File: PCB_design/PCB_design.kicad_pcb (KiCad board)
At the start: 2 copper layers, 39 parts, among them J1 USB_B_Micro, J4 Conn_01x02_Pin, Q1 FS8205A, U1 L298N, U2 L7805, U3 TP4056, U4 DW01A

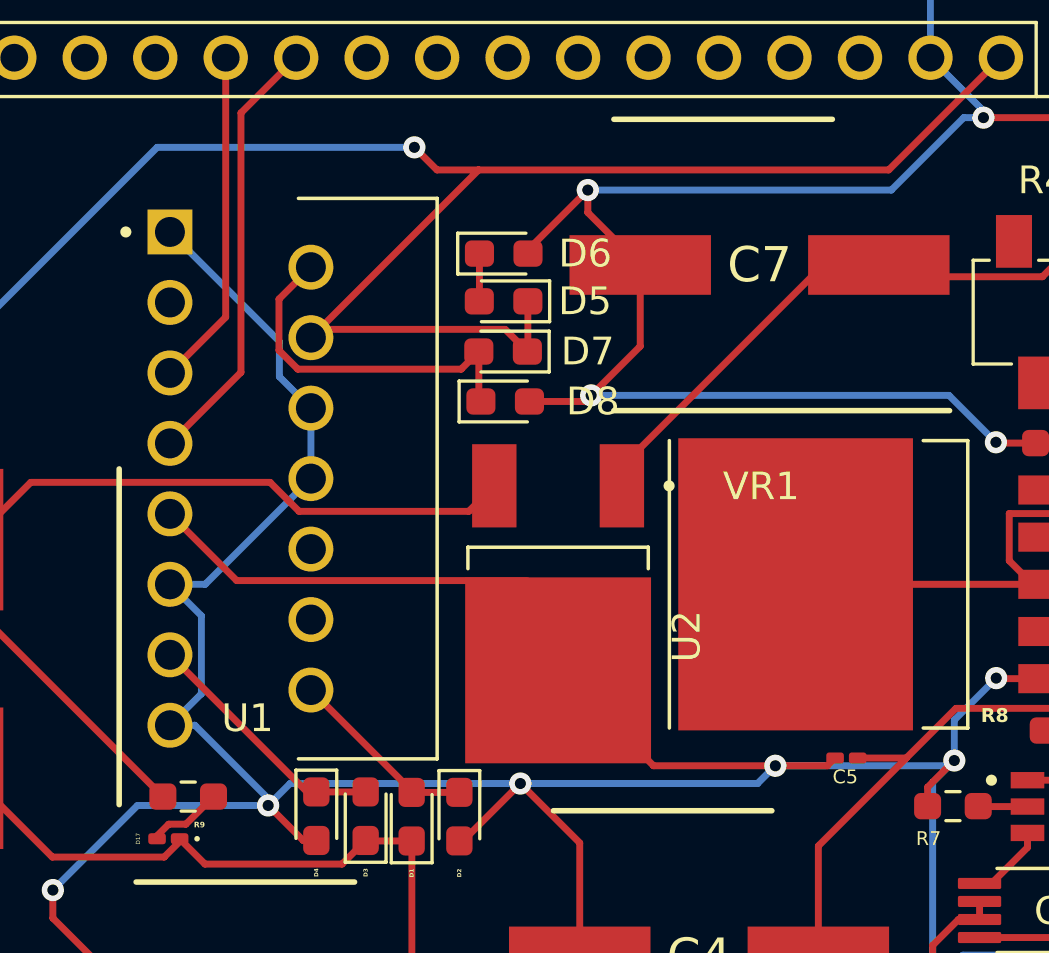
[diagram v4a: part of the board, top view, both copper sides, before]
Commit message: Fixed issues surrounding wiring, Vss to Vs for 12V, CE actually enabled
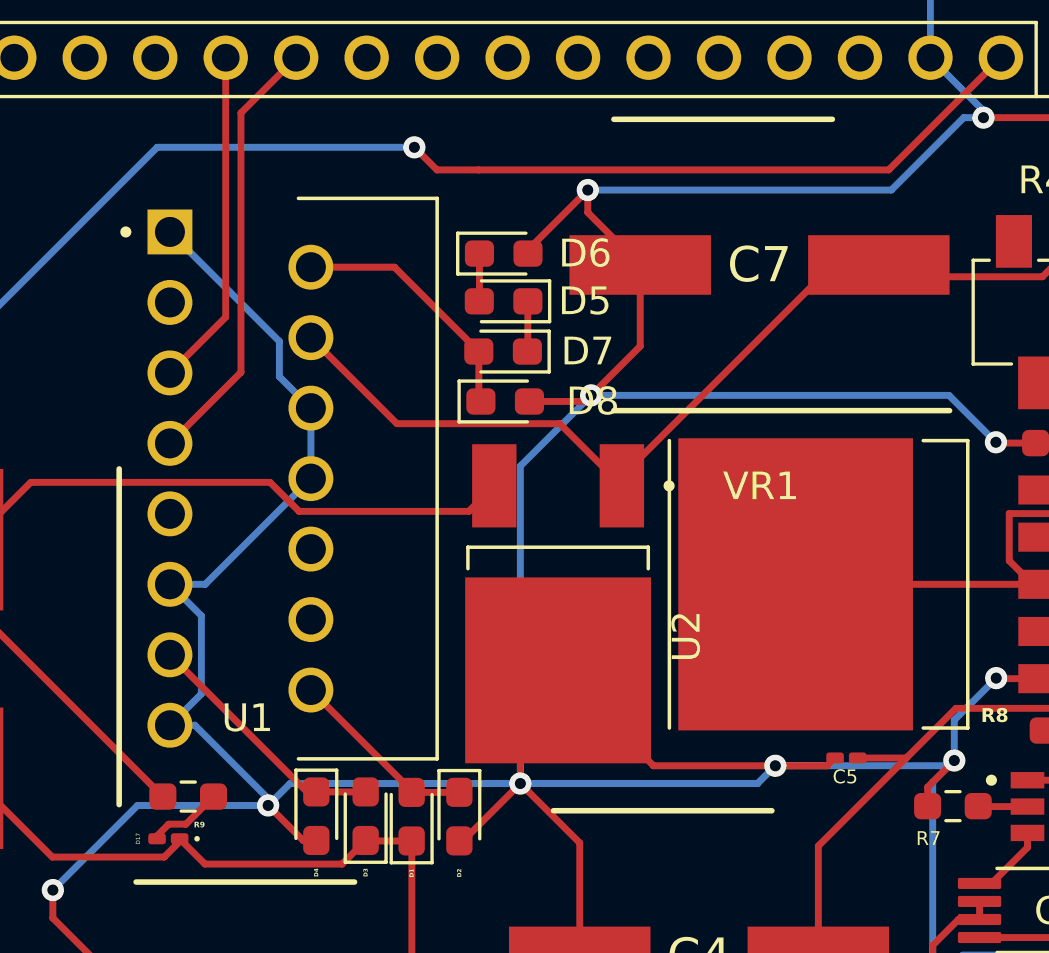
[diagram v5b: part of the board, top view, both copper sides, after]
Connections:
- U1 pad 4: +5V -> Boost_Out
- U1 pad 9: GND_Out -> +5V
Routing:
- net +5V: track 104.3 -> 87.5 mm
- net Boost_Out: track 28.5 -> 44.5 mm
- net GND_Out: track 232.0 -> 237.8 mm
- net OUT1: track 13.0 -> 9.14 mm
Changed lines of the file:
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@@
       (net 37 "OUT2") (pinfunction "OUT2") (pintype "output") (solder_mask_margin 0.102))
     (pad "4" thru_hole circle (at 5.08 3.81) (size 1.62 1.62) (drill 1.08) (layers "*.Cu" "*.Mask")
-      (net 28 "+5V") (pinfunction "Vs") (pintype "power_in") (solder_mask_margin 0.102))
+      (net 31 "Boost_Out") (pinfunction "Vs") (pintype "power_in") (solder_mask_margin 0.102))
     (pad "5" thru_hole circle (at 0 5.08) (size 1.62 1.62) (drill 1.08) (layers "*.Cu" "*.Mask")
       (net 18 "Net-(A1-A0)") (pinfunction "IN1") (pintype "input") (solder_mask_margin 0.102))
@@
       (net 61 "GND_Out") (pinfunction "GND") (pintype "power_in") (solder_mask_margin 0.102))
     (pad "9" thru_hole circle (at 0 10.16) (size 1.62 1.62) (drill 1.08) (layers "*.Cu" "*.Mask")
-      (net 61 "GND_Out") (pinfunction "Vss") (pintype "power_in") (solder_mask_margin 0.102))
+      (net 28 "+5V") (pinfunction "Vss") (pintype "power_in") (solder_mask_margin 0.102))
     (pad "10" thru_hole circle (at 5.08 11.43) (size 1.62 1.62) (drill 1.08) (layers "*.Cu" "*.Mask")
       (net 56 "unconnected-(U1-IN3-Pad10)") (pinfunction "IN3") (pintype "input") (solder_mask_margin 0.102))
@@
   (segment (start 145.36125 91.3) (end 143.7215 91.3) (width 0.25) (layer "F.Cu") (net 28))
   (segment (start 137 91.323541) (end 136.443541 91.88) (width 0.25) (layer "F.Cu") (net 28))
-  (segment (start 149.5325 73.66) (end 148.7325 72.86) (width 0.25) (layer "F.Cu") (net 28))
   (segment (start 145.37 97.64) (end 144.98 98.03) (width 0.25) (layer "F.Cu") (net 28))
   (segment (start 132.41 91.88) (end 129.57 89.04) (width 0.25) (layer "F.Cu") (net 28))
@@
   (segment (start 147.775 67.115) (end 146.275 67.115) (width 0.25) (layer "F.Cu") (net 28))
   (segment (start 137.9125 92.1325) (end 142.854 92.1325) (width 0.25) (layer "F.Cu") (net 28))
-  (segment (start 147.775 67.115) (end 141.73 73.16) (width 0.25) (layer "F.Cu") (net 28))
   (segment (start 146.275 67.115) (end 145.46 66.3) (width 0.25) (layer "F.Cu") (net 28))
   (segment (start 149.55 71.85) (end 149.55 73.6425) (width 0.25) (layer "F.Cu") (net 28))
@@
   (segment (start 145.37 91.30875) (end 145.37 97.64) (width 0.25) (layer "F.Cu") (net 28))
   (segment (start 137 91.22) (end 137 91.323541) (width 0.25) (layer "F.Cu") (net 28))
-  (segment (start 148.7325 72.86) (end 142.03 72.86) (width 0.25) (layer "F.Cu") (net 28))
   (segment (start 149.55 73.6425) (end 149.5325 73.66) (width 0.25) (layer "F.Cu") (net 28))
   (segment (start 137 91.22) (end 137.9125 92.1325) (width 0.25) (layer "F.Cu") (net 28))
   (segment (start 136.443541 91.88) (end 132.41 91.88) (width 0.25) (layer "F.Cu") (net 28))
-  (segment (start 142.03 72.86) (end 141.73 73.16) (width 0.25) (layer "F.Cu") (net 28))
   (segment (start 142.854 92.1325) (end 143.704 91.2825) (width 0.25) (layer "F.Cu") (net 28))
   (segment (start 145.36125 91.3) (end 145.37 91.30875) (width 0.25) (layer "F.Cu") (net 28))
@@
   (segment (start 169.15 86.52) (end 169.95 87.32) (width 0.25) (layer "F.Cu") (net 30))
   (segment (start 162.625 70.965) (end 168.095 70.965) (width 0.25) (layer "F.Cu") (net 31))
+  (segment (start 141.73 73.16) (end 144.83 76.26) (width 0.25) (layer "F.Cu") (net 31))
   (segment (start 174.27 71.08) (end 171.74 71.08) (width 0.25) (layer "F.Cu") (net 31))
   (segment (start 170.76 71.08) (end 169.37 69.69) (width 0.25) (layer "F.Cu") (net 31))
   (segment (start 171.74 68.86) (end 171.74 71.08) (width 0.25) (layer "F.Cu") (net 31))
   (segment (start 168.095 70.965) (end 169.37 69.69) (width 0.25) (layer "F.Cu") (net 31))
+  (segment (start 152.94 78.5) (end 152.94 78.15) (width 0.25) (layer "F.Cu") (net 31))
   (segment (start 160.2 70.54) (end 162.2 70.54) (width 0.25) (layer "F.Cu") (net 31))
-  (segment (start 152.94 77.8) (end 160.2 70.54) (width 0.25) (layer "F.Cu") (net 31))
+  (segment (start 160.55 70.54) (end 162.2 70.54) (width 0.25) (layer "F.Cu") (net 31))
   (segment (start 152.94 78.5) (end 152.94 77.8) (width 0.25) (layer "F.Cu") (net 31))
   (segment (start 171.74 71.08) (end 170.76 71.08) (width 0.25) (layer "F.Cu") (net 31))
+  (segment (start 152.94 78.15) (end 160.55 70.54) (width 0.25) (layer "F.Cu") (net 31))
   (segment (start 162.2 70.54) (end 162.625 70.965) (width 0.25) (layer "F.Cu") (net 31))
+  (segment (start 150.7 76.26) (end 152.94 78.5) (width 0.25) (layer "F.Cu") (net 31))
+  (segment (start 144.83 76.26) (end 150.7 76.26) (width 0.25) (layer "F.Cu") (net 31))
   (segment (start 170.42925 101.66) (end 170.42725 101.662) (width 0.25) (layer "F.Cu") (net 32))
   (segment (start 166.35225 100.709) (end 167.30325 101.66) (width 0.25) (layer "F.Cu") (net 32))
@@
   (segment (start 147.805 70.13) (end 147.805 71.845) (width 0.25) (layer "F.Cu") (net 37))
   (segment (start 147.805 71.845) (end 147.8 71.85) (width 0.25) (layer "F.Cu") (net 37))
+  (segment (start 144.7425 70.62) (end 147.7825 73.66) (width 0.25) (layer "F.Cu") (net 38))
   (segment (start 147.7825 75.385) (end 147.8575 75.46) (width 0.25) (layer "F.Cu") (net 38))
   (segment (start 147.7825 73.66) (end 147.7825 75.385) (width 0.25) (layer "F.Cu") (net 38))
-  (segment (start 147.1475 74.295) (end 141.259867 74.295) (width 0.25) (layer "F.Cu") (net 38))
-  (segment (start 140.58 71.77) (end 141.73 70.62) (width 0.25) (layer "F.Cu") (net 38))
-  (segment (start 140.58 73.615133) (end 140.58 71.77) (width 0.25) (layer "F.Cu") (net 38))
-  (segment (start 141.259867 74.295) (end 140.58 73.615133) (width 0.25) (layer "F.Cu") (net 38))
-  (segment (start 147.7825 73.66) (end 147.1475 74.295) (width 0.25) (layer "F.Cu") (net 38))
+  (segment (start 141.73 70.62) (end 144.7425 70.62) (width 0.25) (layer "F.Cu") (net 38))
   (segment (start 176.13925 97.439505) (end 176.13925 98.615) (width 0.25) (layer "F.Cu") (net 39))
   (segment (start 175.202245 96.5025) (end 176.13925 97.439505) (width 0.25) (layer "F.Cu") (net 39))
@@
   (segment (start 163.9575 89.3625) (end 164.92 88.4) (width 0.25) (layer "F.Cu") (net 61))
   (segment (start 141.926 91.2825) (end 141.4525 91.2825) (width 0.25) (layer "F.Cu") (net 61))
+  (segment (start 150.64 85.15) (end 149.28 86.51) (width 0.25) (layer "F.Cu") (net 61))
   (segment (start 166.35225 96.899) (end 164.539 96.899) (width 0.25) (layer "F.Cu") (net 61))
   (segment (start 149.555 70.13) (end 149.555 69.995) (width 0.25) (layer "F.Cu") (net 61))
@@
   (segment (start 173.86975 93.84) (end 173.86975 94.16975) (width 0.25) (layer "F.Cu") (net 61))
   (segment (start 136.38 98.03) (end 132.43 94.08) (width 0.25) (layer "F.Cu") (net 61))
-  (segment (start 139.055 81.915) (end 136.65 79.51) (width 0.25) (layer "F.Cu") (net 61))
   (segment (start 132.43 94.08) (end 132.43 93.07) (width 0.25) (layer "F.Cu") (net 61))
   (segment (start 151.71 68.65) (end 151.71 67.84) (width 0.25) (layer "F.Cu") (net 61))
@@
   (segment (start 163.36925 98.650495) (end 163.36925 97.27075) (width 0.25) (layer "F.Cu") (net 61))
   (segment (start 147.08125 91.2975) (end 147.2125 91.2975) (width 0.25) (layer "F.Cu") (net 61))
-  (segment (start 149.525 81.915) (end 139.055 81.915) (width 0.25) (layer "F.Cu") (net 61))
   (segment (start 173.86975 94.16975) (end 174.42 94.72) (width 0.25) (layer "F.Cu") (net 61))
   (segment (start 166.45 85.45) (end 166.43 85.43) (width 0.25) (layer "F.Cu") (net 61))
   (segment (start 153.6 73.47) (end 151.83 75.24) (width 0.25) (layer "F.Cu") (net 61))
   (segment (start 168.83 85.45) (end 166.45 85.45) (width 0.25) (layer "F.Cu") (net 61))
+  (segment (start 149.28 86.51) (end 149.28 89.23) (width 0.25) (layer "F.Cu") (net 61))
   (segment (start 165.83 94.13) (end 165.06967 94.13) (width 0.25) (layer "F.Cu") (net 61))
   (segment (start 147.2125 91.2975) (end 149.28 89.23) (width 0.25) (layer "F.Cu") (net 61))
@@
   (segment (start 164.73 88.59) (end 158.47 88.59) (width 0.25) (layer "B.Cu") (net 61))
   (segment (start 164.73 75.24) (end 166.42 76.93) (width 0.25) (layer "B.Cu") (net 61))
+  (segment (start 149.28 89.23) (end 149.28 77.79) (width 0.25) (layer "B.Cu") (net 61))
   (segment (start 149.28 89.23) (end 157.83 89.23) (width 0.25) (layer "B.Cu") (net 61))
   (segment (start 164.14 89.18) (end 164.92 88.4) (width 0.25) (layer "B.Cu") (net 61))
   (segment (start 165.26 65.23) (end 162.65 67.84) (width 0.25) (layer "B.Cu") (net 61))
   (segment (start 162.65 67.84) (end 151.71 67.84) (width 0.25) (layer "B.Cu") (net 61))
+  (segment (start 149.28 77.79) (end 151.83 75.24) (width 0.25) (layer "B.Cu") (net 61))
   (segment (start 149.28 89.23) (end 140.98 89.23) (width 0.25) (layer "B.Cu") (net 61))
   (segment (start 164.06 52.91) (end 158.98 47.83) (width 0.25) (layer "B.Cu") (net 61))

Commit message: Update Read.MD
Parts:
- moved D2 23.5 mm to (129.6, 74.7), turned to 0 degrees
- moved D1 21.1 mm to (129.6, 76.4), turned to 180 degrees
- moved D5 19.1 mm to (129.6, 72.9)
- moved D6 19.1 mm to (129.6, 71.1)
- moved D7 15.3 mm to (133.6, 76.3)
- moved D8 15.1 mm to (133.7, 74.6)
- moved R3 10.4 mm to (166.3, 66.9), turned to -90 degrees
- moved C6 8.96 mm to (163.7, 67.8)
- moved D9 3.94 mm to (170.7, 72.9)
- moved R4 3.66 mm to (164.6, 72.5)
- moved C7 3.60 mm to (154.3, 70.7)
- moved D17 1.24 mm to (137.8, 91.2), turned to 0 degrees
- turned C1 to 90 degrees
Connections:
- A1 pad 21: unconnected-(A1-A2-Pad21) -> Net-(A1-A2)
- A1 pad 22: unconnected-(A1-A3-Pad22) -> Net-(A1-A3)
- A1 pad 27: unconnected-(A1-+5V-Pad27) -> +5V
- A1 pad 30: +5V -> unconnected-(A1-VIN-Pad30)
- C1 pad 2: +5V -> Net-(D1-K)
- C2 pad 1: +5V -> Net-(D1-K)
- C8 pad 1: Net-(J1-VBUS) -> Net-(D10-A)
- D1 pad 1: +5V -> Net-(D1-K)
- D17 pad 1: +5V -> GND_Out
- D3 pad 1: +5V -> Net-(D1-K)
- D5 pad 1: +5V -> Net-(D1-K)
- D7 pad 1: +5V -> Net-(D1-K)
- J1 pad 1: Net-(J1-VBUS) -> Net-(D10-A)
- U1 pad 10: unconnected-(U1-IN3-Pad10) -> Net-(A1-A2)
- U1 pad 11: GND_Out -> +5V
- U1 pad 12: unconnected-(U1-IN4-Pad12) -> Net-(A1-A3)
- U1 pad 6: GND_Out -> +5V
- U1 pad 9: +5V -> Net-(D1-K)
- U3 pad 4: Net-(J1-VBUS) -> Net-(D10-A)
- U3 pad 9: unconnected-(U3-EP-Pad9) -> GND_Out
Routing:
- net GND_Out: track 237.8 -> 0.00 mm, vias 12 -> 0
- net +5V: track 87.5 -> 0.00 mm, vias 2 -> 0
- net Net-(D1-K): track 0.00 -> 59.7 mm
- net Bat+: track 53.4 -> 0.00 mm
- net Boost_Out: track 44.5 -> 0.00 mm
- net Net-(D9-B): track 30.2 -> 11.0 mm
- net Batt-: track 18.9 -> 0.00 mm, vias 2 -> 0
- net Net-(A1-A1): track 15.8 -> 0.00 mm
- net Net-(A1-A0): track 12.2 -> 0.00 mm
- net OUT1: track 9.14 -> 0.00 mm
- net OUT3: track 9.10 -> 0.00 mm
- net Net-(U4-OD): track 7.53 -> 0.00 mm
- net OUT4: track 6.92 -> 0.00 mm
- net Net-(U2-OUT): track 32.5 -> 25.9 mm
- net Net-(D10-A): track 6.33 -> 0.00 mm
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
